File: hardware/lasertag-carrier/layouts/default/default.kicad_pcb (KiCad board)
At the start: 2 copper layers, 100 x 80 mm, 38 parts, among them J0 Power in 2P, J1 S3-Matrix L, J12 Ext button, J13 Touch hdr, J14 Activity LED, J2 S3-Matrix R, J3 MAX98357A, J5 microSD, J6 IR RX, J7 IR LED, J8 WS2812 out, J9 OLED I2C, Q1 2N2222A, SW1 SW_PUSH_6mm, SW2 PWR switch

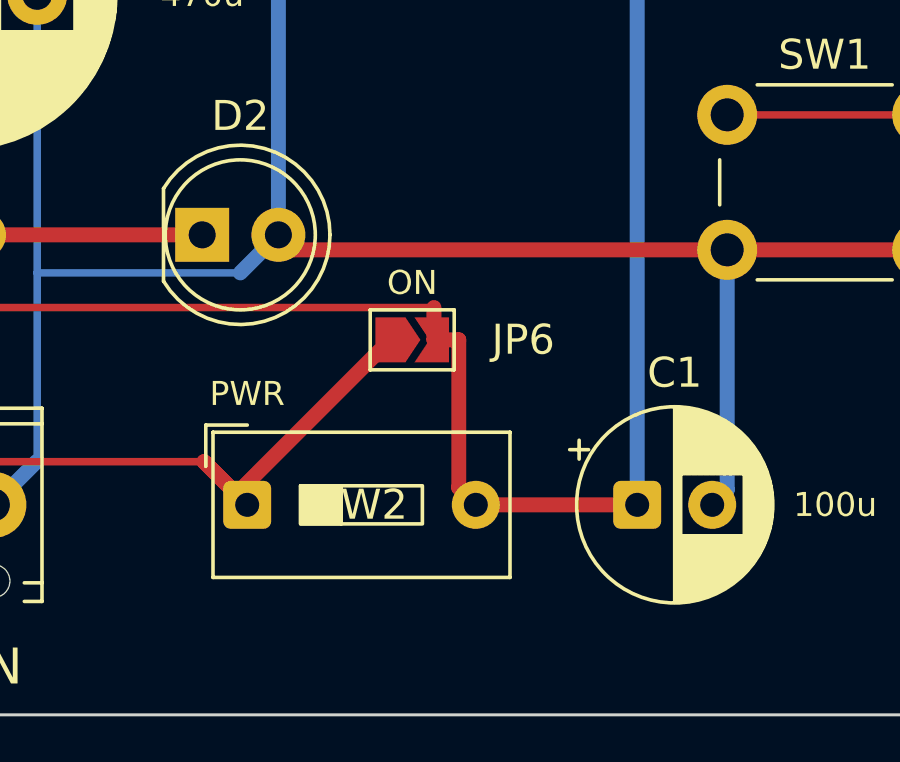
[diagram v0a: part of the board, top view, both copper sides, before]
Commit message: SW2 ref lower in body; restore D2's function label as PWR LED
- SW2 refdes moved to the lower half of the switch body, clear of the
  actuator silk
- "PWR LED" added right of D2 (its function label was lost when the
  ambiguous PWR text was removed). D1 is intentionally absent from the
  carrier: the spec assigns D1 to the IR emitter LED, which is off-board
  on a cable into J7.

DRC: 0 unconnected, 0 electrical, down to the single J6 phantom warning.
Fab zip regenerated.

Co-Authored-By: Claude Opus 4.8 <noreply@anthropic.com>
Claude-Session: https://claude.ai/code/session_01TutNLcDSScdeeVSbjpyg8j
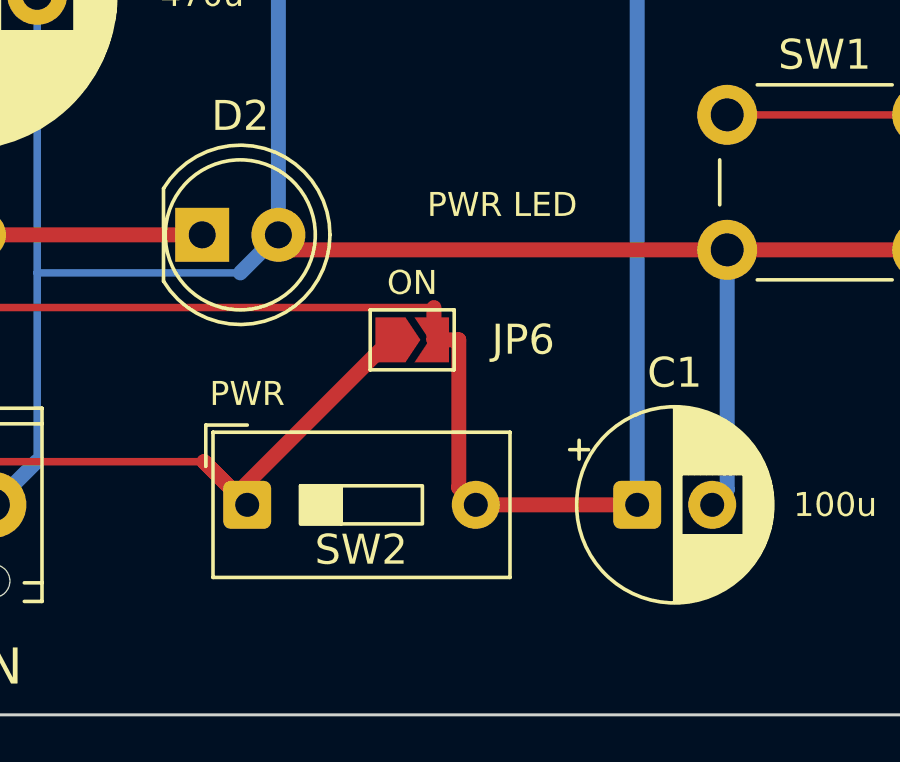
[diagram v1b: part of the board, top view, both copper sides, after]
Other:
- board text added: "PWR LED"
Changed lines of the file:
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@@
 		(tags "DIP Switch SPST Slide 7.62mm 300mil")
 		(property "Reference" "SW2"
-			(at 3.8 0 0)
+			(at 3.8 1.5 0)
 			(layer "F.SilkS")
 			(effects
@@
 			)
 		)
+	)
+	(gr_text "PWR LED"
+		(at 131.5 123 0)
+		(layer "F.SilkS")
+		(effects
+			(font
+				(size 0.8 0.8)
+				(thickness 0.13)
+			)
+		)

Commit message: Silk: D1 marker at IR LED header, J5 ref to socket corner, hide H1-H4
- "D1" under J7 so the off-board IR emitter's designator appears where
  it plugs in
- J5 refdes moved to the socket's bottom-right, beneath the microSD label
- H1-H4 mounting hole refs hidden (self-evident; only needed in BOM)

DRC: single J6 phantom warning only. Fab zip regenerated.

Co-Authored-By: Claude Opus 4.8 <noreply@anthropic.com>
Claude-Session: https://claude.ai/code/session_01TutNLcDSScdeeVSbjpyg8j
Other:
- board text added: "D1"
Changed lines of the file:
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@@
 		(at 187.5 115)
 		(property "Reference" "J5"
-			(at -4 16.8 0)
+			(at 3.4 12.5 0)
 			(layer "F.SilkS")
 			(effects
@@
 		(property "Reference" "H4"
 			(at 0 -4.15 0)
+			(hide yes)
 			(layer "F.SilkS")
 			(effects
@@
 		(property "Reference" "H1"
 			(at 0 4.2 0)
+			(hide yes)
 			(layer "F.SilkS")
 			(effects
@@
 		(property "Reference" "H2"
 			(at 0 4.2 0)
+			(hide yes)
 			(layer "F.SilkS")
 			(effects
@@
 		(property "Reference" "H3"
 			(at 0 -4.15 0)
+			(hide yes)
 			(layer "F.SilkS")
 			(effects
@@
 		(layer "F.SilkS")
 		(effects
+			(font
+				(size 0.8 0.8)
+				(thickness 0.13)
+			)
+		)
+	)
+	(gr_text "D1"
+		(at 188 68.9 0)
+		(layer "F.SilkS")
+		(effects
